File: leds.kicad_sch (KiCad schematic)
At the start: 7 parts, among them IC36 SN74AHCT1G125DBVR

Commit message: [FIX](General) footprints
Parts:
- IC36: footprint SOT95P280X145-5N -> SN74AHCT1G125DBVR:SOT95P280X145-5N
- renumbered R9 to R15
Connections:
- net Din renamed LED_DATA
- net GND renamed LED_GND
- net Vcc renamed LED_5V
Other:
- sheet LED ports: added VCC; removed VDD
- sheet LED1 ports: added VCC; removed VDD
- sheet LED10 ports: added VCC; removed VDD
- sheet LED11 ports: added VCC; removed VDD
- sheet LED12 ports: added VCC; removed VDD
- sheet LED13 ports: added VCC; removed VDD
- sheet LED14 ports: added VCC; removed VDD
- sheet LED15 ports: added VCC; removed VDD
- sheet LED16 ports: added VCC; removed VDD
- sheet LED17 ports: added VCC; removed VDD
- sheet LED18 ports: added VCC; removed VDD
- sheet LED19 ports: added VCC; removed VDD
- sheet LED2 ports: added VCC; removed VDD
- sheet LED20 ports: added VCC; removed VDD
- sheet LED21 ports: added VCC; removed VDD
- sheet LED22 ports: added VCC; removed VDD
- sheet LED23 ports: added VCC; removed VDD
- sheet LED24 ports: added VCC; removed VDD
- sheet LED25 ports: added VCC; removed VDD
- sheet LED26 ports: added VCC; removed VDD
- sheet LED27 ports: added VCC; removed VDD
- sheet LED28 ports: added VCC; removed VDD
- sheet LED29 ports: added VCC; removed VDD
- sheet LED3 ports: added VCC; removed VDD
- sheet LED30 ports: added VCC; removed VDD
- sheet LED31 ports: added VCC; removed VDD
- sheet LED4 ports: added VCC; removed VDD
- sheet LED5 ports: added VCC; removed VDD
- sheet LED6 ports: added VCC; removed VDD
- sheet LED7 ports: added VCC; removed VDD
- sheet LED8 ports: added VCC; removed VDD
- sheet LED9 ports: added VCC; removed VDD

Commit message: [ADD](General) added all footprints expect leds
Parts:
- C70, C71, C72, C73, C74: footprint (none) -> Capacitor_SMD:C_0603_1608Metric_Pad1.08x0.95mm_HandSolder
- R15: footprint (none) -> Resistor_SMD:R_0603_1608Metric_Pad0.98x0.95mm_HandSolder
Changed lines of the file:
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@@
 			)
 		)
-		(property "Footprint" ""
+		(property "Footprint" "Resistor_SMD:R_0603_1608Metric_Pad0.98x0.95mm_HandSolder"
 			(at 93.98 170.688 90)
 			(effects
@@
 			)
 		)
-		(property "Footprint" ""
+		(property "Footprint" "Capacitor_SMD:C_0603_1608Metric_Pad1.08x0.95mm_HandSolder"
 			(at 213.6648 91.44 0)
 			(effects
@@
 			)
 		)
-		(property "Footprint" ""
+		(property "Footprint" "Capacitor_SMD:C_0603_1608Metric_Pad1.08x0.95mm_HandSolder"
 			(at 215.5952 88.9 0)
 			(effects
@@
 			)
 		)
-		(property "Footprint" ""
+		(property "Footprint" "Capacitor_SMD:C_0603_1608Metric_Pad1.08x0.95mm_HandSolder"
 			(at 213.6648 128.27 0)
 			(effects
@@
 			)
 		)
-		(property "Footprint" ""
+		(property "Footprint" "Capacitor_SMD:C_0603_1608Metric_Pad1.08x0.95mm_HandSolder"
 			(at 213.6648 44.45 0)
 			(effects
@@
 			)
 		)
-		(property "Footprint" ""
+		(property "Footprint" "Capacitor_SMD:C_0603_1608Metric_Pad1.08x0.95mm_HandSolder"
 			(at 86.6648 173.99 0)
 			(effects

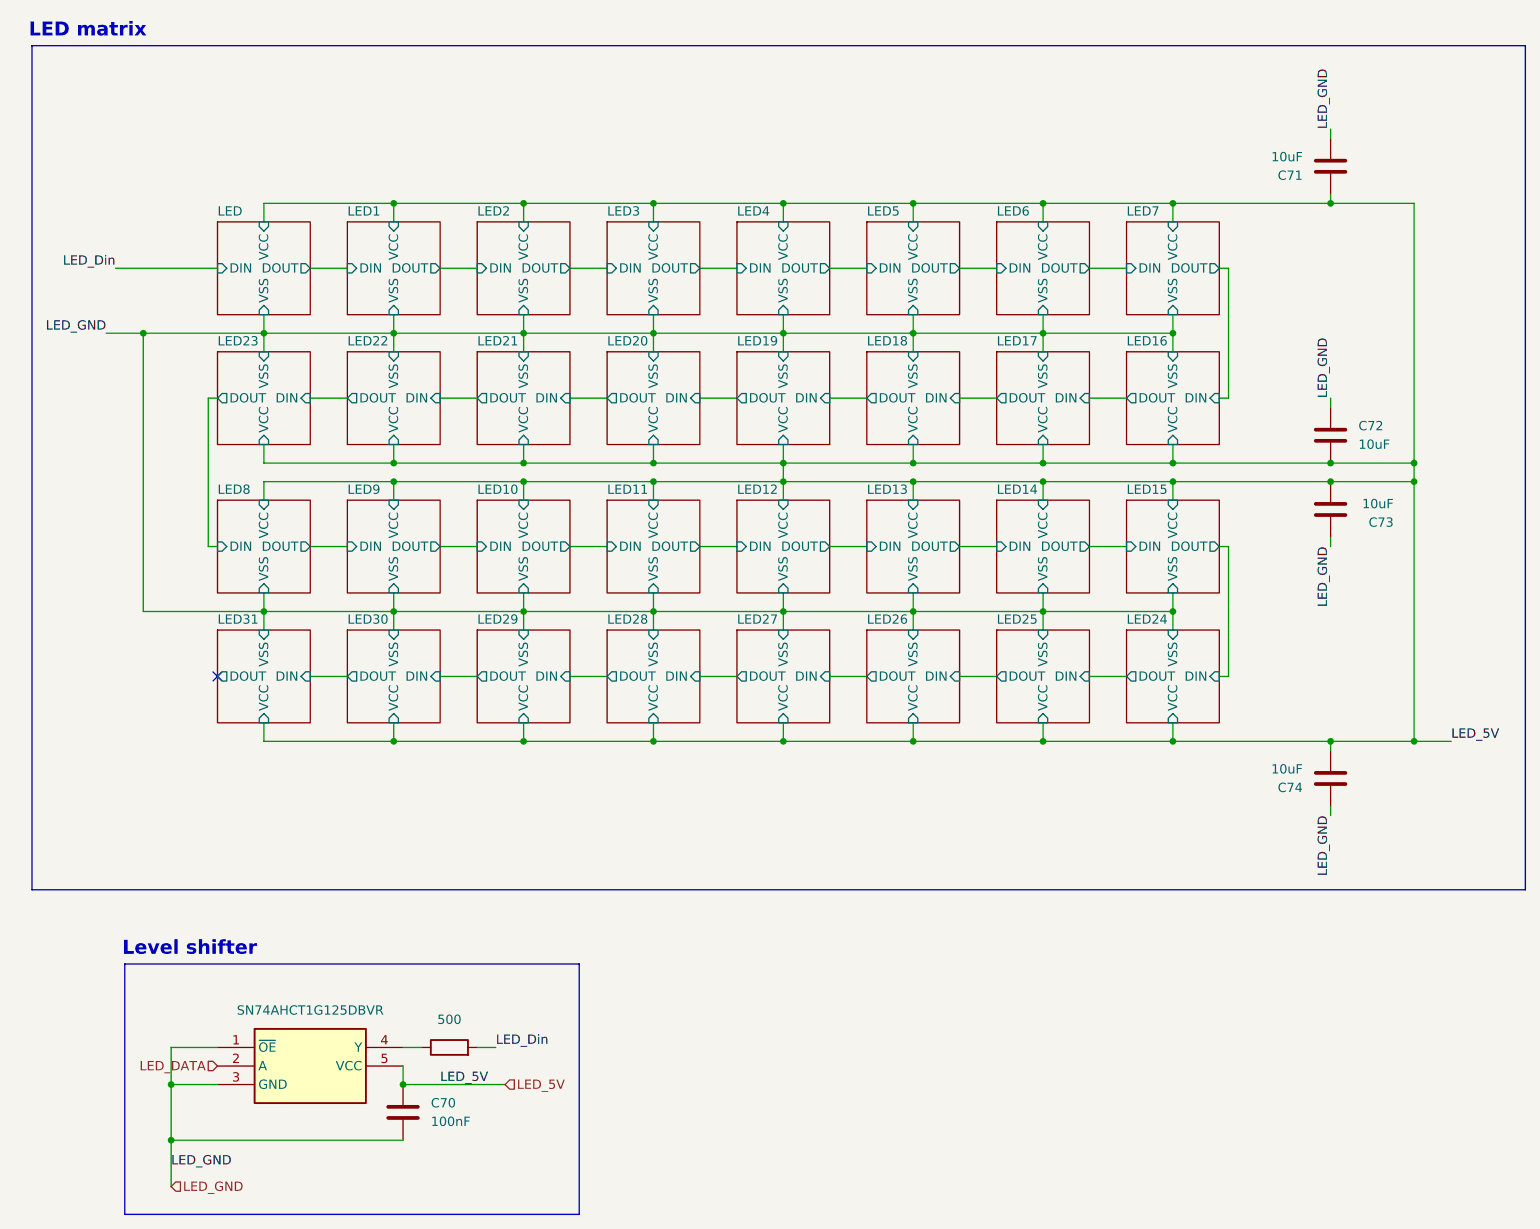
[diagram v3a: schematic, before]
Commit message: [FIX](USB) main usb net labels
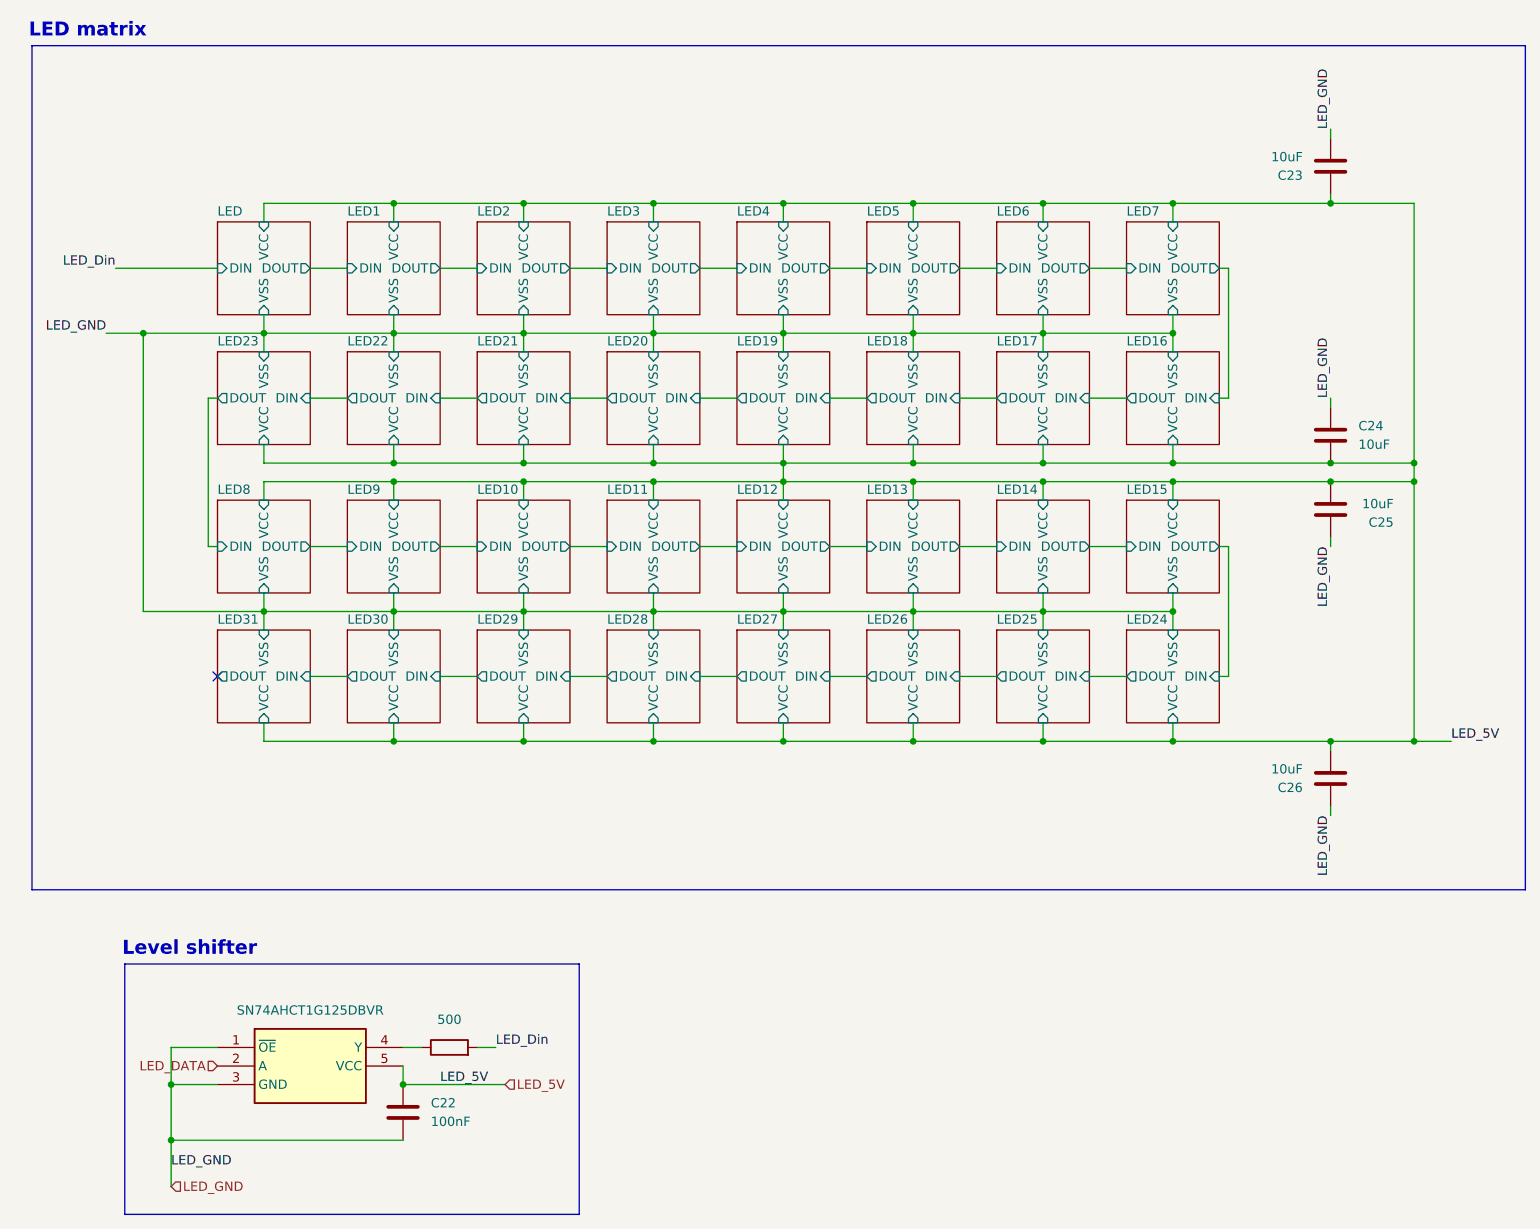
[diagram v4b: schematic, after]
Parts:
- renumbered C70 to C22, C71 to C23, C72 to C24, C73 to C25, C74 to C26, IC36 to IC3, R15 to R9
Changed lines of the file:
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@@
 		(dnp no)
 		(fields_autoplaced yes)
-		(property "Reference" "R15"
+		(property "Reference" "R9"
 			(at 93.98 162.56 90)
 			(effects
@@
 			(project "RyzzenKeyboard"
 				(path "/5d44d704-6136-40a8-98a4-93f001ea8743/ddd39123-7c60-4daf-80ad-ae6eff6f8029"
-					(reference "R15")
+					(reference "R9")
 					(unit 1)
 				)
@@
 		(dnp no)
 		(fields_autoplaced yes)
-		(property "Reference" "IC36"
+		(property "Reference" "IC3"
 			(at 74.93 161.29 0)
 			(effects
@@
 			(project ""
 				(path "/5d44d704-6136-40a8-98a4-93f001ea8743/ddd39123-7c60-4daf-80ad-ae6eff6f8029"
-					(reference "IC36")
+					(reference "IC3")
 					(unit 1)
 				)
@@
 		(on_board yes)
 		(dnp no)
-		(property "Reference" "C73"
+		(property "Reference" "C25"
 			(at 223.266 97.028 0)
 			(effects
@@
 			(project "RyzzenKeyboard"
 				(path "/5d44d704-6136-40a8-98a4-93f001ea8743/ddd39123-7c60-4daf-80ad-ae6eff6f8029"
-					(reference "C73")
+					(reference "C25")
 					(unit 1)
 				)
@@
 		(dnp no)
 		(fields_autoplaced yes)
-		(property "Reference" "C72"
+		(property "Reference" "C24"
 			(at 218.44 83.8199 0)
 			(effects
@@
 			(project "RyzzenKeyboard"
 				(path "/5d44d704-6136-40a8-98a4-93f001ea8743/ddd39123-7c60-4daf-80ad-ae6eff6f8029"
-					(reference "C72")
+					(reference "C24")
 					(unit 1)
 				)
@@
 		(dnp no)
 		(fields_autoplaced yes)
-		(property "Reference" "C74"
+		(property "Reference" "C26"
 			(at 210.82 133.3501 0)
 			(effects
@@
 			(project "RyzzenKeyboard"
 				(path "/5d44d704-6136-40a8-98a4-93f001ea8743/ddd39123-7c60-4daf-80ad-ae6eff6f8029"
-					(reference "C74")
+					(reference "C26")
 					(unit 1)
 				)
@@
 		(dnp no)
 		(fields_autoplaced yes)
-		(property "Reference" "C71"
+		(property "Reference" "C23"
 			(at 210.82 49.5301 0)
 			(effects
@@
 			(project "RyzzenKeyboard"
 				(path "/5d44d704-6136-40a8-98a4-93f001ea8743/ddd39123-7c60-4daf-80ad-ae6eff6f8029"
-					(reference "C71")
+					(reference "C23")
 					(unit 1)
 				)
@@
 		(on_board yes)
 		(dnp no)
-		(property "Reference" "C70"
+		(property "Reference" "C22"
 			(at 91.44 176.5299 0)
 			(effects
@@
 			(project "RyzzenKeyboard"
 				(path "/5d44d704-6136-40a8-98a4-93f001ea8743/ddd39123-7c60-4daf-80ad-ae6eff6f8029"
-					(reference "C70")
-					(unit 1)
-				)
+					(reference "C22")
+					(unit 1)
+				)

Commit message: [ADD](PCB) led and tmr caps placement
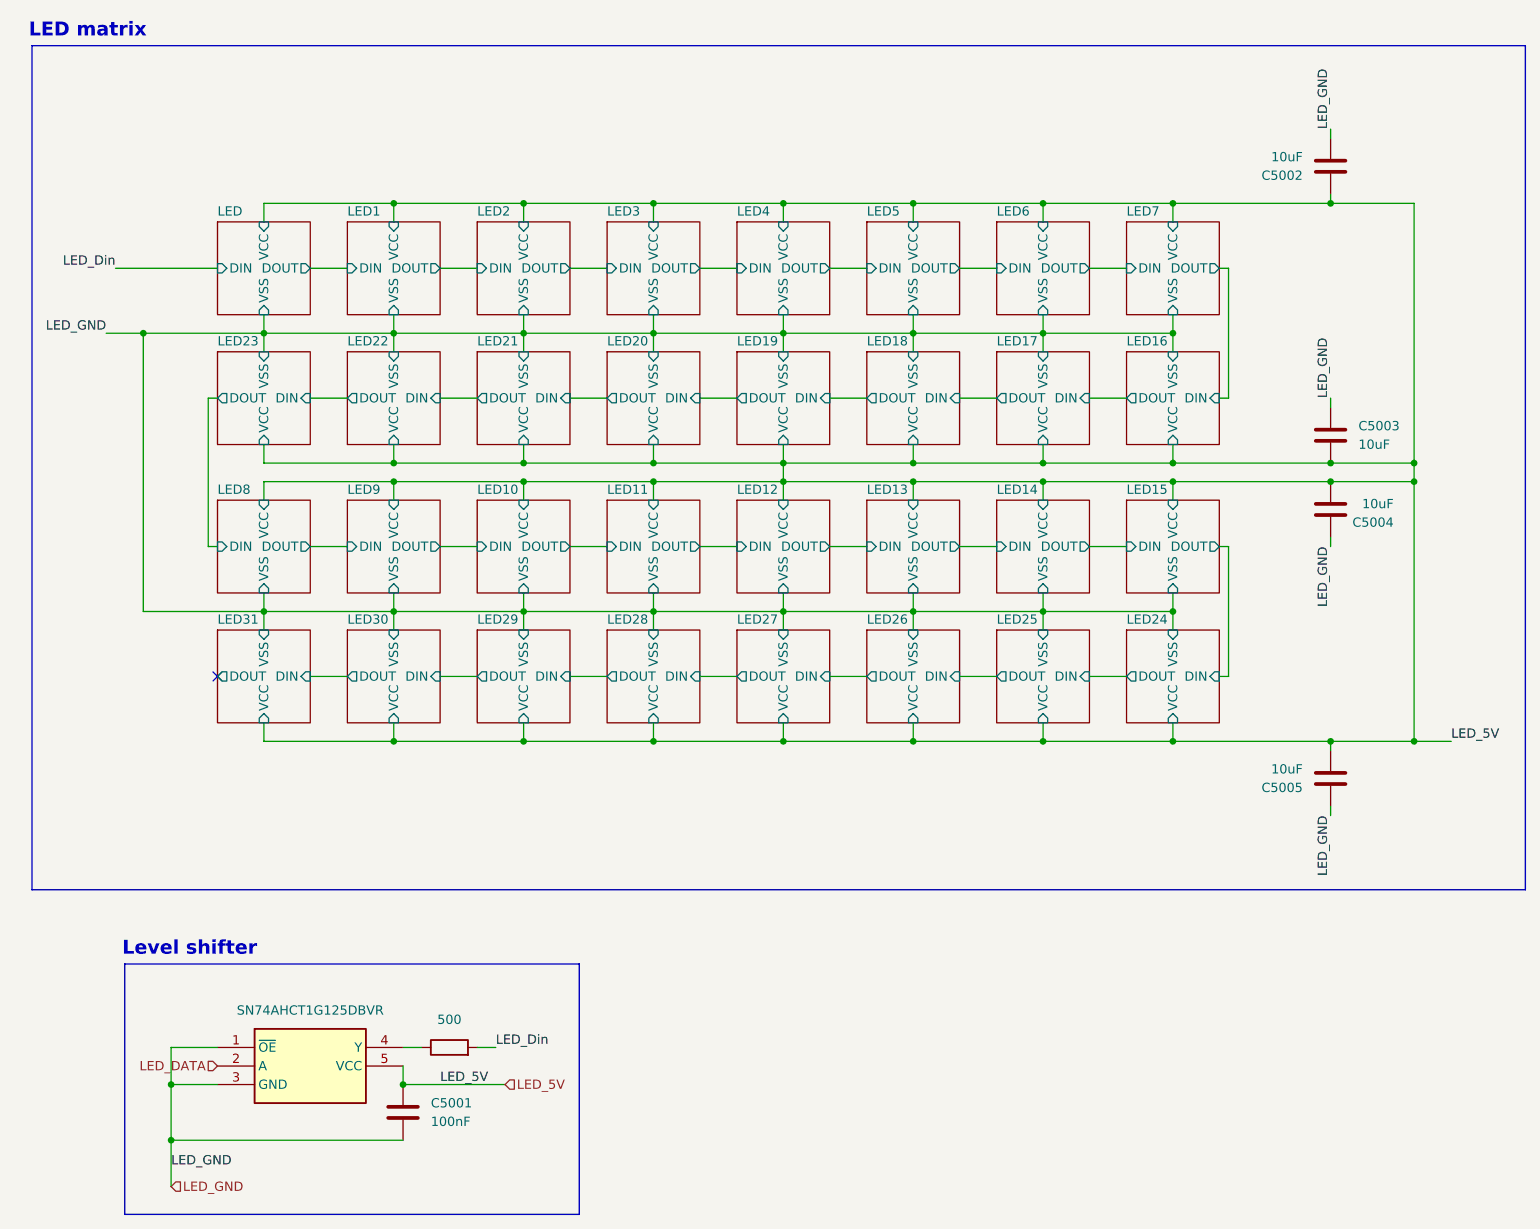
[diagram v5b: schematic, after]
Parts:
- renumbered C22 to C5001, C23 to C5002, C24 to C5003, C25 to C5004, C26 to C5005, IC3 to IC5001, R9 to R5001
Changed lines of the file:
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@@
 		(dnp no)
 		(fields_autoplaced yes)
-		(property "Reference" "R9"
+		(property "Reference" "R5001"
 			(at 93.98 162.56 90)
 			(effects
@@
 			(project "RyzzenKeyboard"
 				(path "/5d44d704-6136-40a8-98a4-93f001ea8743/ddd39123-7c60-4daf-80ad-ae6eff6f8029"
-					(reference "R9")
+					(reference "R5001")
 					(unit 1)
 				)
@@
 		(dnp no)
 		(fields_autoplaced yes)
-		(property "Reference" "IC3"
+		(property "Reference" "IC5001"
 			(at 74.93 161.29 0)
 			(effects
@@
 			(project ""
 				(path "/5d44d704-6136-40a8-98a4-93f001ea8743/ddd39123-7c60-4daf-80ad-ae6eff6f8029"
-					(reference "IC3")
+					(reference "IC5001")
 					(unit 1)
 				)
@@
 		(on_board yes)
 		(dnp no)
-		(property "Reference" "C25"
+		(property "Reference" "C5004"
 			(at 223.266 97.028 0)
 			(effects
@@
 			(project "RyzzenKeyboard"
 				(path "/5d44d704-6136-40a8-98a4-93f001ea8743/ddd39123-7c60-4daf-80ad-ae6eff6f8029"
-					(reference "C25")
+					(reference "C5004")
 					(unit 1)
 				)
@@
 		(dnp no)
 		(fields_autoplaced yes)
-		(property "Reference" "C24"
+		(property "Reference" "C5003"
 			(at 218.44 83.8199 0)
 			(effects
@@
 			(project "RyzzenKeyboard"
 				(path "/5d44d704-6136-40a8-98a4-93f001ea8743/ddd39123-7c60-4daf-80ad-ae6eff6f8029"
-					(reference "C24")
+					(reference "C5003")
 					(unit 1)
 				)
@@
 		(dnp no)
 		(fields_autoplaced yes)
-		(property "Reference" "C26"
+		(property "Reference" "C5005"
 			(at 210.82 133.3501 0)
 			(effects
@@
 			(project "RyzzenKeyboard"
 				(path "/5d44d704-6136-40a8-98a4-93f001ea8743/ddd39123-7c60-4daf-80ad-ae6eff6f8029"
-					(reference "C26")
+					(reference "C5005")
 					(unit 1)
 				)
@@
 		(dnp no)
 		(fields_autoplaced yes)
-		(property "Reference" "C23"
+		(property "Reference" "C5002"
 			(at 210.82 49.5301 0)
 			(effects
@@
 			(project "RyzzenKeyboard"
 				(path "/5d44d704-6136-40a8-98a4-93f001ea8743/ddd39123-7c60-4daf-80ad-ae6eff6f8029"
-					(reference "C23")
+					(reference "C5002")
 					(unit 1)
 				)
@@
 		(on_board yes)
 		(dnp no)
-		(property "Reference" "C22"
+		(property "Reference" "C5001"
 			(at 91.44 176.5299 0)
 			(effects
@@
 			(project "RyzzenKeyboard"
 				(path "/5d44d704-6136-40a8-98a4-93f001ea8743/ddd39123-7c60-4daf-80ad-ae6eff6f8029"
-					(reference "C22")
+					(reference "C5001")
 					(unit 1)
 				)
@@
 			(project "RyzzenKeyboard"
 				(path "/5d44d704-6136-40a8-98a4-93f001ea8743/ddd39123-7c60-4daf-80ad-ae6eff6f8029"
-					(page "105")
+					(page "109")
 				)
 			)
@@
 			(project "RyzzenKeyboard"
 				(path "/5d44d704-6136-40a8-98a4-93f001ea8743/ddd39123-7c60-4daf-80ad-ae6eff6f8029"
-					(page "109")
+					(page "107")
 				)
 			)
@@
 			(project "RyzzenKeyboard"
 				(path "/5d44d704-6136-40a8-98a4-93f001ea8743/ddd39123-7c60-4daf-80ad-ae6eff6f8029"
-					(page "6")
-				)
-			)
+					(page "108")
+				)
+			)

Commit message: [ADD](Mountinghole)
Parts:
- removed C5002, C5003, C5004, C5005: 10uF, Capacitor_SMD:C_0603_1608Metric_Pad1.08x0.95mm_HandSolder, symbol Device:C
